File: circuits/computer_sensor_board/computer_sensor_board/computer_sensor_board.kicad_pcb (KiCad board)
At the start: 2 copper layers, 100 x 50 mm, 11 parts, among them J1 Conn_Main_DCDC, J2 Conn_Jetson, J5 Conn_VLP16, J6 Conn_Main_DCDC, U1 TDN_5-2411WISM, U2 Teensy4.1, U3 MCP3425_DIP

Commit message: design board
Signed-off-by: Masaya Kataoka <ms.kataoka@gmail.com>
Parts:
- removed J1: Conn_Main_DCDC, Connector_AMASS:AMASS_XT30PW-F_1x02_P2.50mm_Horizontal
- removed R1: 120K, Resistor_THT:R_Axial_DIN0207_L6.3mm_D2.5mm_P10.16mm_Horizontal
- removed R2: 20K, Resistor_THT:R_Axial_DIN0207_L6.3mm_D2.5mm_P10.16mm_Horizontal
- removed R3, R4: 4.7K, Resistor_THT:R_Axial_DIN0207_L6.3mm_D2.5mm_P10.16mm_Horizontal
- removed U3: MCP3425_DIP, Package_TO_SOT_SMD:SOT-23-6
- added J7: Conn_Router, Connector_AMASS:AMASS_XT30PW-F_1x02_P2.50mm_Horizontal, F.Cu at (205.0, 64.2)
- added M78AR12-1: ~, M78AR15:M78AR15, F.Cu at (199.0, 74.0)
- U1: value TDN_5-2411WISM -> ~; footprint Converter_DCDC:Converter_DCDC_TRACO_TDN_5-xxxxWISM_SMD -> 5075AR-04-WH:5075AR-04-WH
- U2: value Teensy4.1 -> ~; footprint Teensy:Teensy41 -> 5075AR-04-WH:5075AR-04-WH
- moved U1 62.6 mm to (221.0, 84.5)
- moved U2 50.1 mm to (204.0, 84.5)
- moved J6 37.5 mm to (185.0, 64.0)
- moved J5 10.00 mm to (220.0, 64.2)
- moved J2 8.40 mm to (190.0, 81.0), turned to 180 degrees
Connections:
- J5 pad 1: Net-(J5-Pin_1) -> Net-(J2-Pin_1)
- J6 pad 1: Net-(J2-Pin_2) -> Net-(J2-Pin_1)
- J6 pad 2: Net-(J2-Pin_1) -> Net-(J2-Pin_2)
- U1 pad 1: Net-(J2-Pin_1) -> Net-(M78AR12-1-Vout)
- U1 pad 2: Net-(J2-Pin_2) -> unconnected-(U1-D--Pad2)
- U1 pad 4: unconnected-(U1-ON/OFF-Pad4) -> Net-(J2-Pin_2)
- U2 pad 1: Net-(J3-GND) -> Net-(M78AR12-1-Vout)
- U2 pad 4: unconnected-(U2-2_OUT2-Pad4) -> Net-(J2-Pin_2)
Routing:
- net Net-(J2-Pin_2): track 0.00 -> 108.0 mm
- net Net-(M78AR12-1-Vout): track 0.00 -> 91.1 mm
- net Net-(J2-Pin_1): track 0.00 -> 71.8 mm
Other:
- board size 100 x 50 mm -> 50 x 35 mm

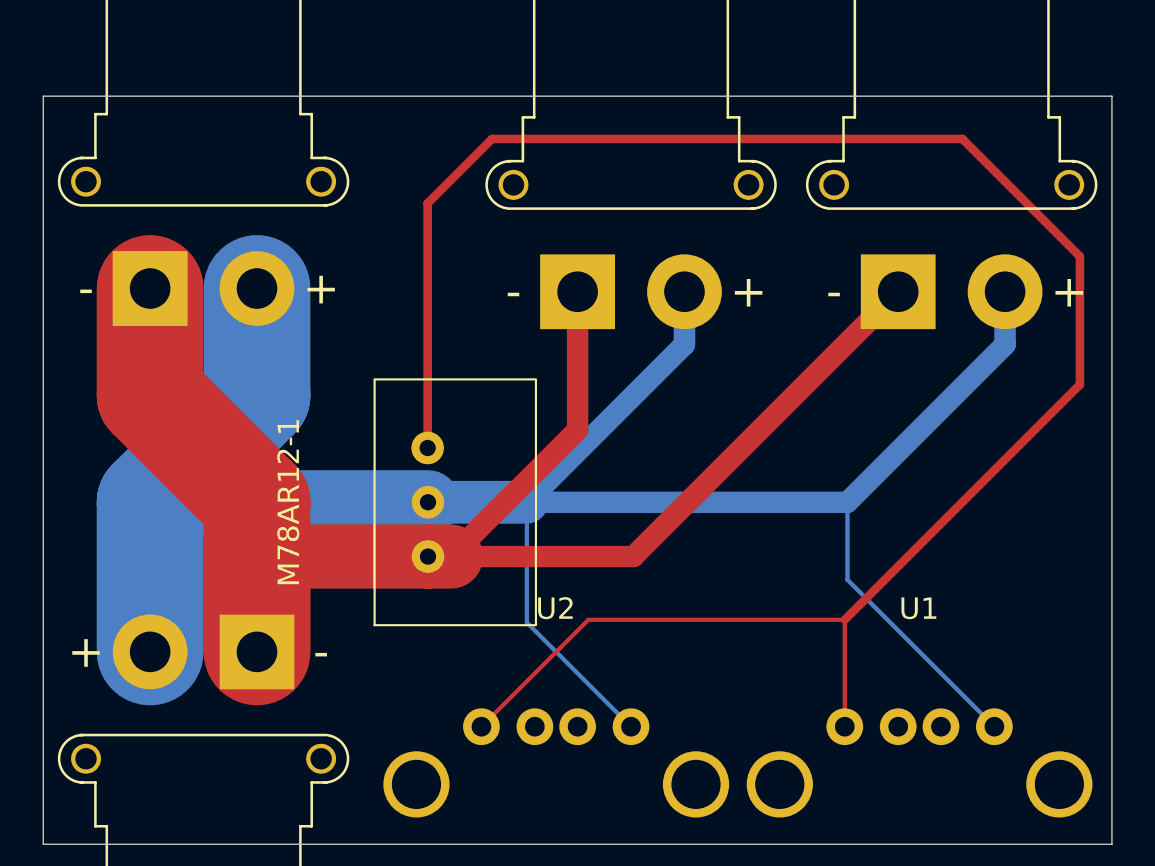
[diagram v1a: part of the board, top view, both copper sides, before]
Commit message: Fix/ad converter type (#361)
* add M78AR05 ad converter

Signed-off-by: Masaya Kataoka <ms.kataoka@gmail.com>

* update design

Signed-off-by: Masaya Kataoka <ms.kataoka@gmail.com>

---------

Signed-off-by: Masaya Kataoka <ms.kataoka@gmail.com>
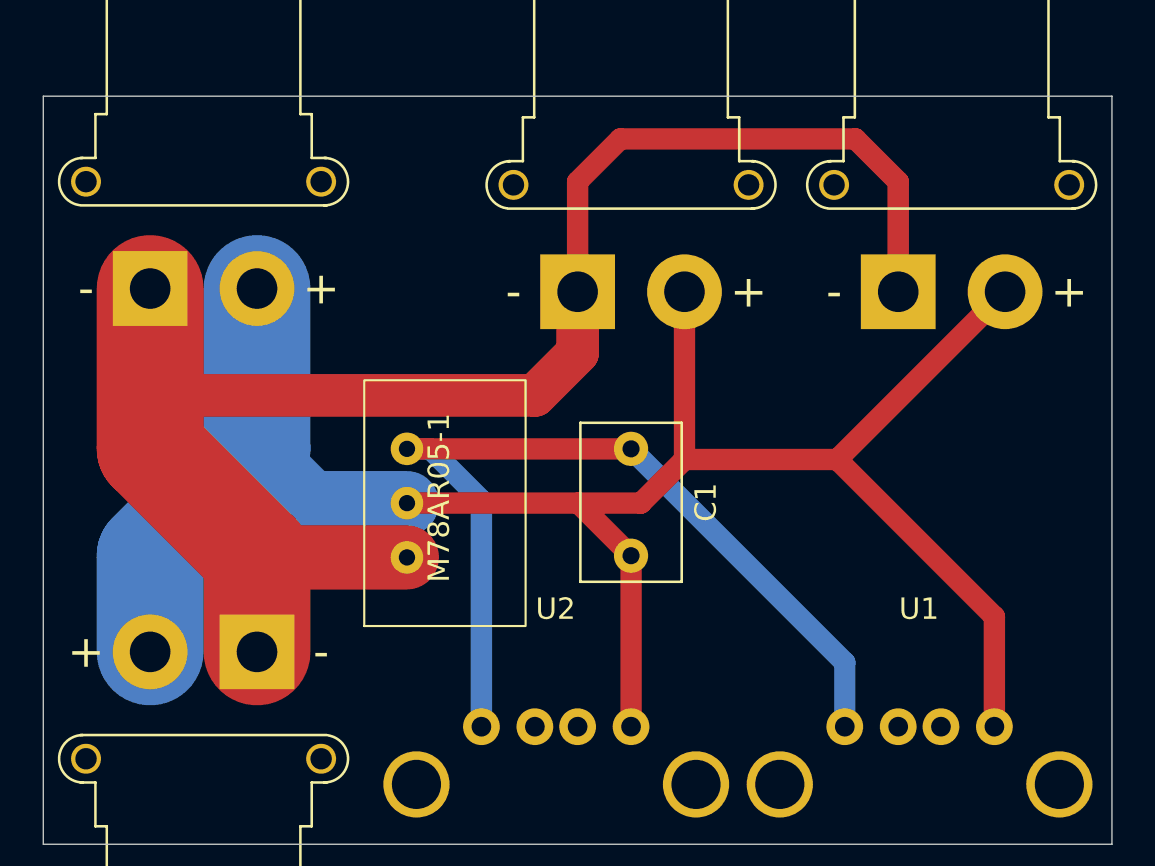
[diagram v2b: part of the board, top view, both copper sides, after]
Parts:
- removed M78AR12-1: ~, M78AR15:M78AR15
- added C1: 3.3uF, Capacitor_THT:C_Rect_L7.2mm_W4.5mm_P5.00mm_FKS2_FKP2_MKS2_MKP2, F.Cu at (207.5, 71.5)
- added M78AR05-1: ~, M78AR05-1:M78AR05-1, F.Cu at (199.0, 73.8)
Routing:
- net Net-(M78AR05-1-Vout): track 91.1 -> 42.7 mm
- net Net-(J2-Pin_2): track 108.0 -> 94.1 mm
- net Net-(J2-Pin_1): track 71.8 -> 77.8 mm

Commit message: Feature/motor controller board (#363)
* add miniv_motor_controller_board

Signed-off-by: Masaya Kataoka <ms.kataoka@gmail.com>

* add connectors

Signed-off-by: Masaya Kataoka <ms.kataoka@gmail.com>

* add some footprint

Signed-off-by: Masaya Kataoka <ms.kataoka@gmail.com>

* update connection

Signed-off-by: Masaya Kataoka <ms.kataoka@gmail.com>

* update schematic

Signed-off-by: Masaya Kataoka <ms.kataoka@gmail.com>

* add PCBGOGO Plugin

Signed-off-by: Masaya Kataoka <ms.kataoka@gmail.com>

* add mounting hole

Signed-off-by: Masaya Kataoka <ms.kataoka@gmail.com>

* enable generate gerber

Signed-off-by: Masaya Kataoka <ms.kataoka@gmail.com>

* enable generate drill file

Signed-off-by: Masaya Kataoka <ms.kataoka@gmail.com>

* modify resister

Signed-off-by: Masaya Kataoka <ms.kataoka@gmail.com>

* fix connection

Signed-off-by: Masaya Kataoka <ms.kataoka@gmail.com>

* update text

Signed-off-by: Masaya Kataoka <ms.kataoka@gmail.com>

* add hole

Signed-off-by: Masaya Kataoka <ms.kataoka@gmail.com>

* add RJ45 connector

Signed-off-by: Masaya Kataoka <ms.kataoka@gmail.com>

* add footprint

Signed-off-by: Masaya Kataoka <ms.kataoka@gmail.com>

* add SS-12D00G3 and modify RJLD-260YC1

Signed-off-by: Masaya Kataoka <ms.kataoka@gmail.com>

* update board

Signed-off-by: Masaya Kataoka <ms.kataoka@gmail.com>

* modify circuit

Signed-off-by: Masaya Kataoka <ms.kataoka@gmail.com>

* add 12V DC/DC

Signed-off-by: Masaya Kataoka <ms.kataoka@gmail.com>

* update schematic

Signed-off-by: Masaya Kataoka <ms.kataoka@gmail.com>

* re-design board

Signed-off-by: Masaya Kataoka <ms.kataoka@gmail.com>

* remove R1/R2

Signed-off-by: Masaya Kataoka <ms.kataoka@gmail.com>

* change line width

Signed-off-by: Masaya Kataoka <ms.kataoka@gmail.com>

* modify board

Signed-off-by: Masaya Kataoka <ms.kataoka@gmail.com>

* remove bom

Signed-off-by: Masaya Kataoka <ms.kataoka@gmail.com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
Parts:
- added H1: MountingHole, MountingHole:MountingHole_3.2mm_M3, F.Cu at (175.0, 60.0)
- added H2: MountingHole, MountingHole:MountingHole_3.2mm_M3, F.Cu at (235.0, 60.0)
- added H3: MountingHole, MountingHole:MountingHole_3.2mm_M3, F.Cu at (175.0, 85.0)
- added H4: MountingHole, MountingHole:MountingHole_3.2mm_M3, F.Cu at (235.0, 85.0)
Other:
- board size 50 x 35 mm -> 70 x 35 mm
- rule pad_to_mask_clearance: 0 -> 0.1

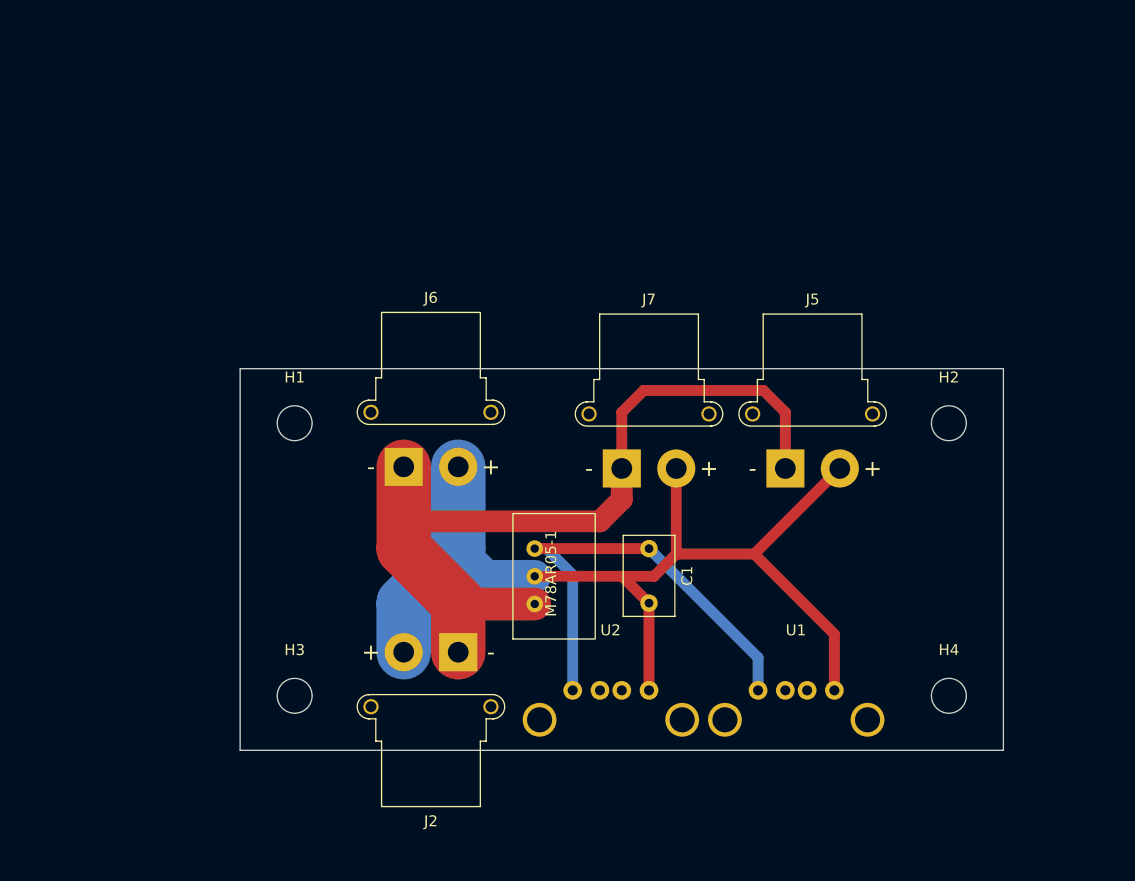
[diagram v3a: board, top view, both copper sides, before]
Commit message: add smart battery
Signed-off-by: Masaya Kataoka <ms.kataoka@gmail.com>
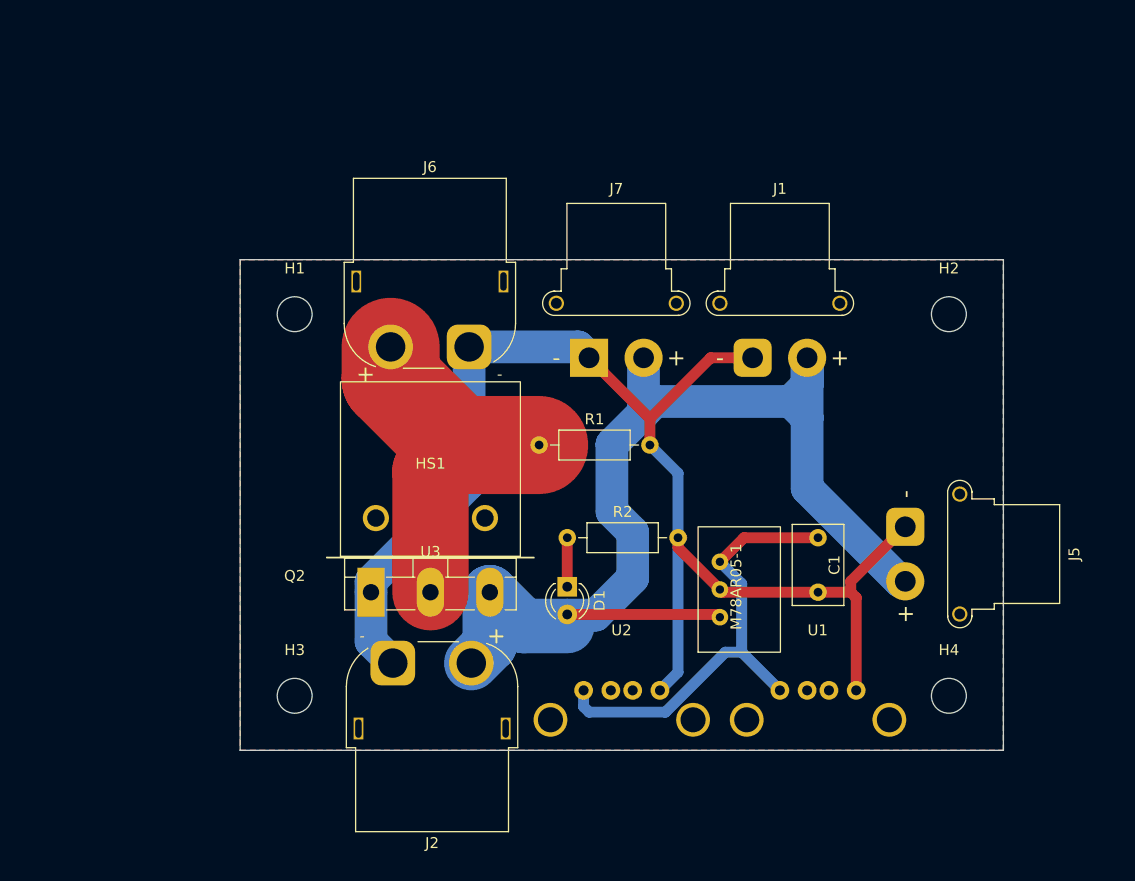
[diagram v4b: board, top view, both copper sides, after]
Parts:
- added D1: LED, LED_THT:LED_D3.0mm, F.Cu at (200.0, 75.0)
- added HS1: Heatsink, 16PB017-01025:16PB017-01025, F.Cu at (187.4, 64.2)
- added J1: Conn_Switching_Hub, Connector_AMASS:AMASS_XT30PW-F_1x02_P2.50mm_Horizontal, F.Cu at (217.0, 54.0)
- added Q2: 2SJ555-E, Package_TO_SOT_THT:TO-3P-3_Vertical, F.Cu at (182.0, 75.5)
- added R1: 100K, Resistor_THT:R_Axial_DIN0207_L6.3mm_D2.5mm_P10.16mm_Horizontal, F.Cu at (197.4, 62.0)
- added R2: 390, Resistor_THT:R_Axial_DIN0207_L6.3mm_D2.5mm_P10.16mm_Horizontal, F.Cu at (200.0, 70.5)
- added U3: Heatsink_sheet, 16PB017-01025:TO-3PH, F.Cu at (187.4, 72.3)
- J2, J6: footprint Connector_AMASS:AMASS_XT30PW-F_1x02_P2.50mm_Horizontal -> Connector_AMASS:AMASS_XT60PW-F_1x02_P7.20mm_Horizontal
- moved M78AR05-1 17.0 mm to (216.0, 75.0)
- moved C1 15.5 mm to (223.0, 70.5)
- moved J6 12.5 mm to (191.0, 53.0)
- moved J5 12.2 mm to (231.0, 69.5), turned to -90 degrees
- moved J7 10.6 mm to (202.0, 54.0)
- moved H1 10.0 mm to (175.0, 50.0)
- moved H2 10.0 mm to (235.0, 50.0)
- moved J2 6.08 mm to (184.0, 82.0)
- moved U1 2.00 mm to (223.0, 84.5)
- moved U2 1.00 mm to (205.0, 84.5)
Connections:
- C1 pad 2: Net-(J2-Pin_2) -> GND
- J2 pad 1: Net-(J2-Pin_1) -> GND
- J2 pad 2: Net-(J2-Pin_2) -> Net-(D1-A)
- J5 pad 1: Net-(J2-Pin_1) -> GND
- J5 pad 2: Net-(J2-Pin_2) -> Net-(D1-A)
- J6 pad 1: Net-(J2-Pin_1) -> GND
- J6 pad 2: Net-(J2-Pin_2) -> Net-(J6-Pin_2)
- J7 pad 1: Net-(J2-Pin_1) -> GND
- J7 pad 2: Net-(J2-Pin_2) -> Net-(D1-A)
- M78AR05-1 pad 1: Net-(J2-Pin_1) -> Net-(D1-A)
- M78AR05-1 pad 2: Net-(J2-Pin_2) -> GND
- U1 pad 4: Net-(J2-Pin_2) -> GND
- U2 pad 4: Net-(J2-Pin_2) -> GND
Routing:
- net GND: track 0.00 -> 127.7 mm
- net Net-(D1-A): track 0.00 -> 108.6 mm
- net Net-(J2-Pin_2): track 94.1 -> 0.00 mm
- net Net-(J2-Pin_1): track 77.8 -> 0.00 mm
- net Net-(J6-Pin_2): track 0.00 -> 33.6 mm
- net Net-(D1-K): track 0.00 -> 4.50 mm
- added copper zone on B.Cu, net GND
- added copper zone on F.Cu, net GND
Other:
- board size 70 x 35 mm -> 70 x 45 mm
